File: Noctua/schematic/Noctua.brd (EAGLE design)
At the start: 30 x 62 mm, 45 parts, among them IC1 PCM3168A, U1 STM32F427V(100PIN), U4 LM3940IMP, X2 53048-05, Y2 8MHz

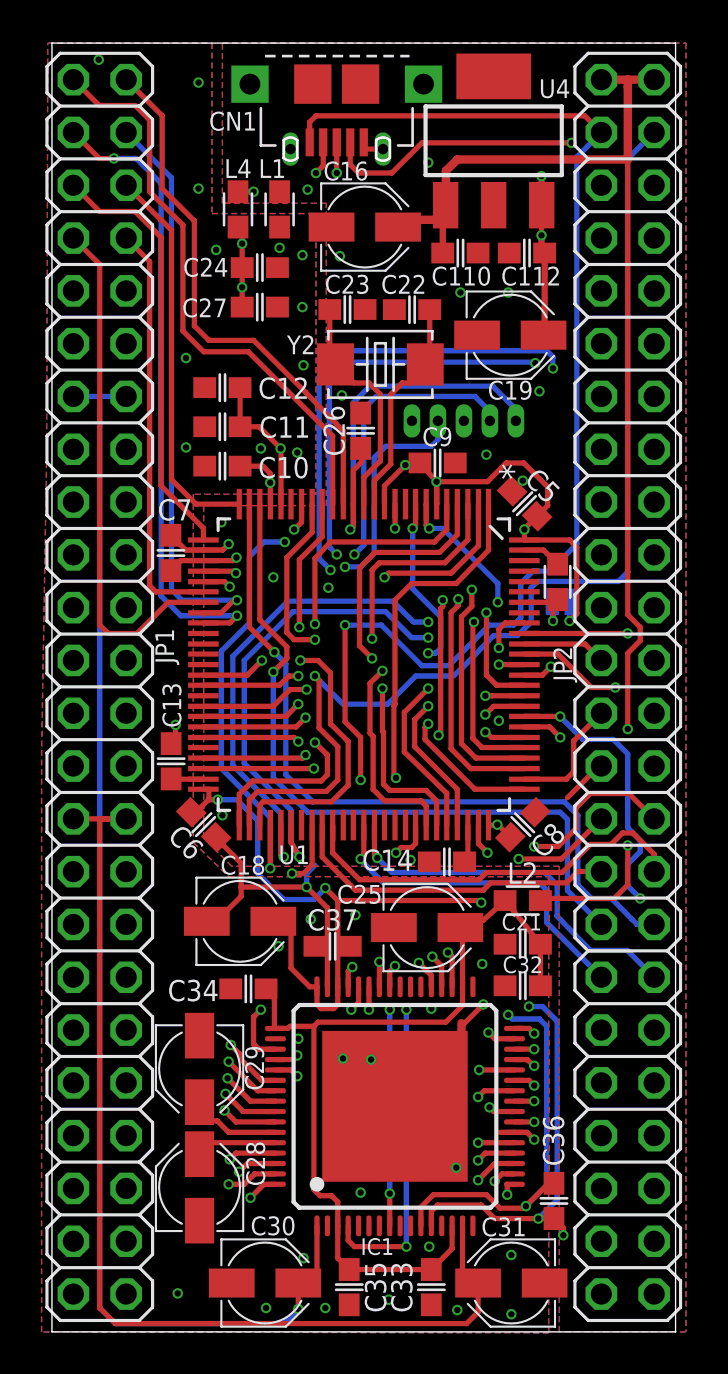
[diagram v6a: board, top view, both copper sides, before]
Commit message: added extra connections for LRCK and BCK to codec
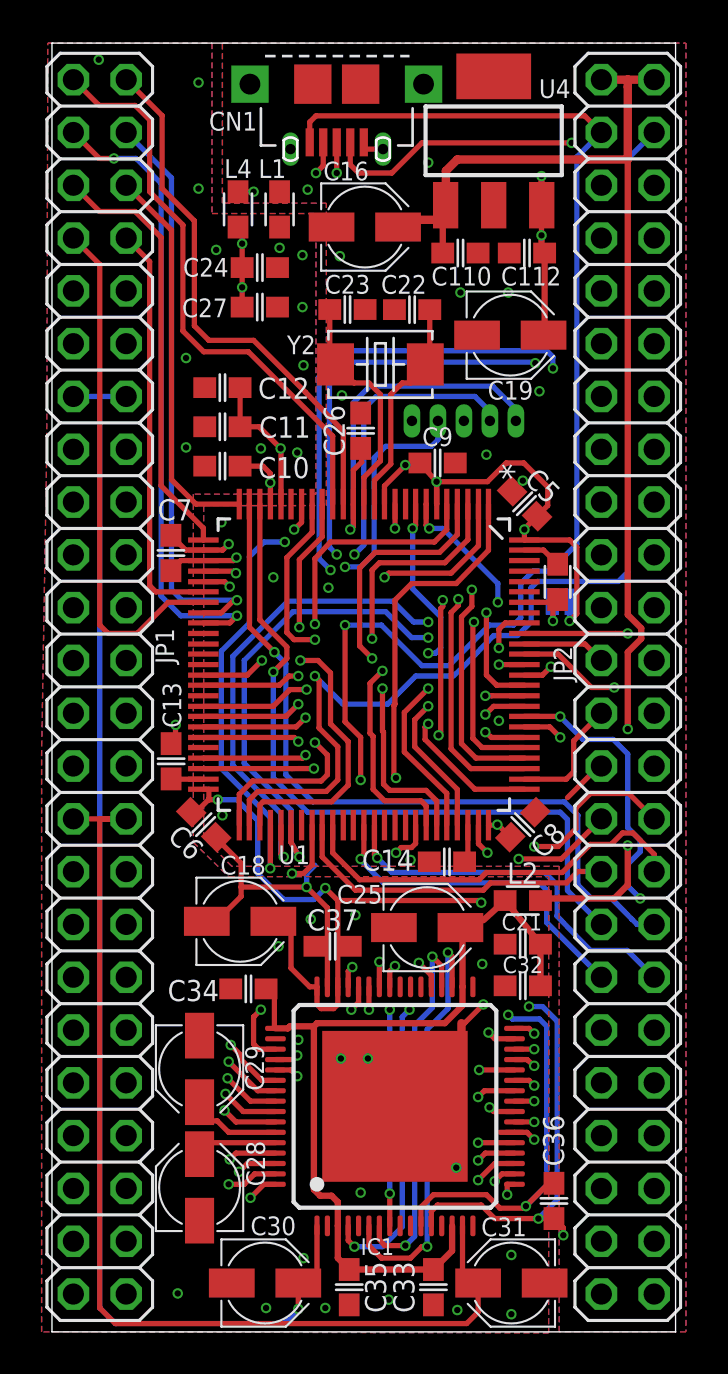
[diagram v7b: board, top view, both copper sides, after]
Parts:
- moved C33 0.10 mm to (18.6, 2.15)
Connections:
- net SAI_BCK: now also IC1.7
- net SAI_LRCK: now also IC1.6
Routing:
- net SAI_LRCK: track 28.9 -> 47.7 mm, vias 2 -> 3
- net SAI_BCK: track 29.3 -> 45.8 mm, vias 2 -> 3
- net ADC_RST: track 43.4 -> 42.8 mm
- net AGND: track 7.24 -> 7.38 mm, vias 32 -> 30

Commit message: changed 47u cap package, changed value naming style
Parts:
- removed L4: 10uH, Rebel:0603
- added L3: 10uH, Rebel:0603
- C16: device Rebel:PANASONIC_B -> Rebel:CPOL-5
- C19: value 10uF -> 10u
- C22, C23: value 20pF -> 22p
- C32, C33, C34, C35, C36, C37: value 1uF -> 1u
- moved L2 36.0 mm to (9.25, 54.0), turned to 90 degrees
- renumbered C110 to C38, C112 to C39, IC1 to U2, U4 to U3, X2 to X1, Y2 to Y1
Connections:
- net +3V3: now also L2.2; no longer L4.2
- net +5V: now also L3.2; no longer L2.2
- net +A3V3: now also L2.1; no longer L4.1
- net +A5V: now also L3.1; no longer L2.1
